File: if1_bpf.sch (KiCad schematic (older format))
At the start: 8 parts

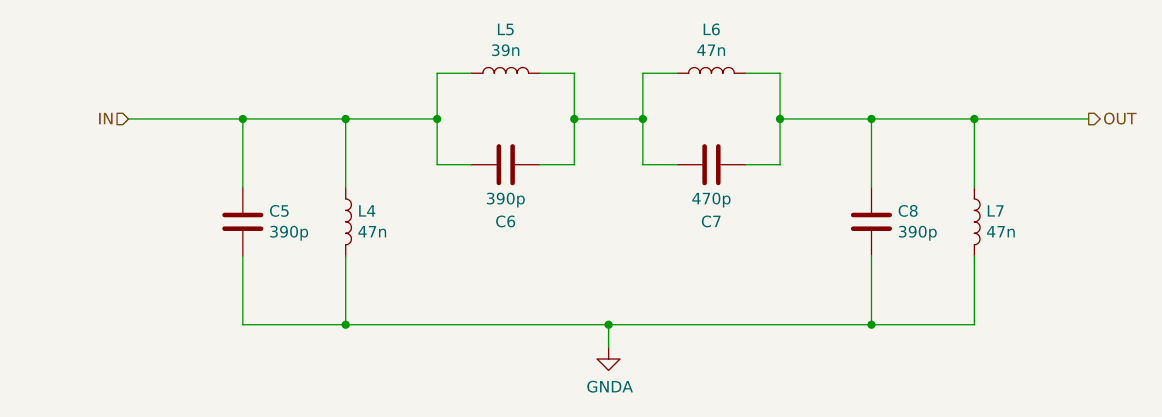
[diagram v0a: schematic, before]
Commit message: FPGA change and new project file
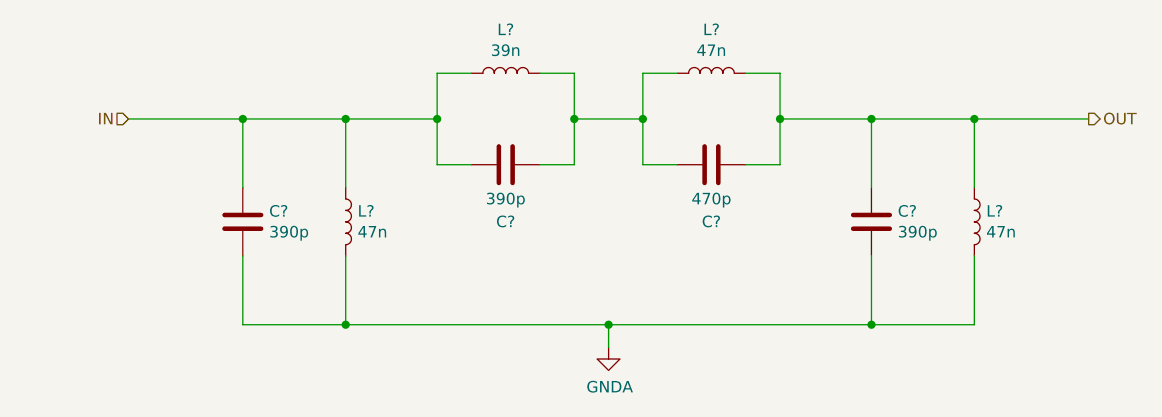
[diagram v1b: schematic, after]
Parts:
- renumbered C5 to C?, C6 to C?, C7 to C?, C8 to C?, L4 to L?, L5 to L?, L6 to L?, L7 to L?
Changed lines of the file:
@@
 $Descr A4 11693 8268
 encoding utf-8
-Sheet 3 7
+Sheet 3 12
 Title "37,224 MHz Bandpass filter"
 Date "2021 january"
@@
 OUT
 $Comp
-L Device:C C5
+L Device:C C?
 U 1 1 600431FC
 P 4450 3850
-F 0 "C5" H 4565 3896 50  0000 L CNN
+F 0 "C?" H 4565 3896 50  0000 L CNN
 F 1 "390p" H 4565 3805 50  0000 L CNN
 F 2 "Capacitor_SMD:C_0805_2012Metric_Pad1.18x1.45mm_HandSolder" H 4488 3700 50  0001 C CNN
@@
 $EndComp
 $Comp
-L Device:L L4
+L Device:L L?
 U 1 1 600436A2
 P 4900 3850
-F 0 "L4" H 4952 3896 50  0000 L CNN
+F 0 "L?" H 4952 3896 50  0000 L CNN
 F 1 "47n" H 4952 3805 50  0000 L CNN
 F 2 "Inductor_SMD:L_0603_1608Metric_Pad1.05x0.95mm_HandSolder" H 4900 3850 50  0001 C CNN
@@
 $EndComp
 $Comp
-L Device:L L5
+L Device:L L?
 U 1 1 600471E0
 P 5600 3200
-F 0 "L5" V 5790 3200 50  0000 C CNN
+F 0 "L?" V 5790 3200 50  0000 C CNN
 F 1 "39n" V 5699 3200 50  0000 C CNN
 F 2 "Inductor_SMD:L_0402_1005Metric_Pad0.77x0.64mm_HandSolder" H 5600 3200 50  0001 C CNN
@@
 $EndComp
 $Comp
-L Device:C C6
+L Device:C C?
 U 1 1 6004779D
 P 5600 3600
-F 0 "C6" V 5350 3600 50  0000 C CNN
+F 0 "C?" V 5350 3600 50  0000 C CNN
 F 1 "390p" V 5450 3600 50  0000 C CNN
 F 2 "Capacitor_SMD:C_0805_2012Metric_Pad1.18x1.45mm_HandSolder" H 5638 3450 50  0001 C CNN
@@
 $EndComp
 $Comp
-L Device:L L6
+L Device:L L?
 U 1 1 6004D573
 P 6500 3200
-F 0 "L6" V 6690 3200 50  0000 C CNN
+F 0 "L?" V 6690 3200 50  0000 C CNN
 F 1 "47n" V 6599 3200 50  0000 C CNN
 F 2 "Inductor_SMD:L_0603_1608Metric_Pad1.05x0.95mm_HandSolder" H 6500 3200 50  0001 C CNN
@@
 $EndComp
 $Comp
-L Device:C C7
+L Device:C C?
 U 1 1 6004D579
 P 6500 3600
-F 0 "C7" V 6250 3600 50  0000 C CNN
+F 0 "C?" V 6250 3600 50  0000 C CNN
 F 1 "470p" V 6350 3600 50  0000 C CNN
 F 2 "Capacitor_SMD:C_0805_2012Metric_Pad1.18x1.45mm_HandSolder" H 6538 3450 50  0001 C CNN
@@
 $EndComp
 $Comp
-L Device:C C8
+L Device:C C?
 U 1 1 6004E74D
 P 7200 3850
-F 0 "C8" H 7315 3896 50  0000 L CNN
+F 0 "C?" H 7315 3896 50  0000 L CNN
 F 1 "390p" H 7315 3805 50  0000 L CNN
 F 2 "Capacitor_SMD:C_0805_2012Metric_Pad1.18x1.45mm_HandSolder" H 7238 3700 50  0001 C CNN
@@
 $EndComp
 $Comp
-L Device:L L7
+L Device:L L?
 U 1 1 6004E753
 P 7650 3850
-F 0 "L7" H 7702 3896 50  0000 L CNN
+F 0 "L?" H 7702 3896 50  0000 L CNN
 F 1 "47n" H 7702 3805 50  0000 L CNN
 F 2 "Inductor_SMD:L_0603_1608Metric_Pad1.05x0.95mm_HandSolder" H 7650 3850 50  0001 C CNN
@@
 	6050 4300 7200 4300
 $Comp
-L power:GNDA #PWR0108
+L power:GNDA #PWR?
 U 1 1 60071173
 P 6050 4400
-F 0 "#PWR0108" H 6050 4150 50  0001 C CNN
+F 0 "#PWR?" H 6050 4150 50  0001 C CNN
 F 1 "GNDA" H 6055 4227 50  0000 C CNN
 F 2 "" H 6050 4400 50  0001 C CNN

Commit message: PCB is Done... Needs DRC check
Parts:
- gave numbers to parts that had none: 8
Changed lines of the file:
@@
 $Descr A4 11693 8268
 encoding utf-8
-Sheet 4 14
+Sheet 4 7
 Title "37,224 MHz Bandpass filter"
 Date "2021 january"
@@
 OUT
 $Comp
-L Device:C C?
+L Device:C C5
 U 1 1 600431FC
 P 4450 3850
-F 0 "C?" H 4565 3896 50  0000 L CNN
+F 0 "C5" H 4565 3896 50  0000 L CNN
 F 1 "390p" H 4565 3805 50  0000 L CNN
 F 2 "Capacitor_SMD:C_0805_2012Metric_Pad1.18x1.45mm_HandSolder" H 4488 3700 50  0001 C CNN
@@
 $EndComp
 $Comp
-L Device:L L?
+L Device:L L4
 U 1 1 600436A2
 P 4900 3850
-F 0 "L?" H 4952 3896 50  0000 L CNN
+F 0 "L4" H 4952 3896 50  0000 L CNN
 F 1 "47n" H 4952 3805 50  0000 L CNN
 F 2 "Inductor_SMD:L_0603_1608Metric_Pad1.05x0.95mm_HandSolder" H 4900 3850 50  0001 C CNN
@@
 $EndComp
 $Comp
-L Device:L L?
+L Device:L L5
 U 1 1 600471E0
 P 5600 3200
-F 0 "L?" V 5790 3200 50  0000 C CNN
+F 0 "L5" V 5790 3200 50  0000 C CNN
 F 1 "39n" V 5699 3200 50  0000 C CNN
 F 2 "Inductor_SMD:L_0402_1005Metric_Pad0.77x0.64mm_HandSolder" H 5600 3200 50  0001 C CNN
@@
 $EndComp
 $Comp
-L Device:C C?
+L Device:C C6
 U 1 1 6004779D
 P 5600 3600
-F 0 "C?" V 5350 3600 50  0000 C CNN
+F 0 "C6" V 5350 3600 50  0000 C CNN
 F 1 "390p" V 5450 3600 50  0000 C CNN
 F 2 "Capacitor_SMD:C_0805_2012Metric_Pad1.18x1.45mm_HandSolder" H 5638 3450 50  0001 C CNN
@@
 $EndComp
 $Comp
-L Device:L L?
+L Device:L L6
 U 1 1 6004D573
 P 6500 3200
-F 0 "L?" V 6690 3200 50  0000 C CNN
+F 0 "L6" V 6690 3200 50  0000 C CNN
 F 1 "47n" V 6599 3200 50  0000 C CNN
 F 2 "Inductor_SMD:L_0603_1608Metric_Pad1.05x0.95mm_HandSolder" H 6500 3200 50  0001 C CNN
@@
 $EndComp
 $Comp
-L Device:C C?
+L Device:C C7
 U 1 1 6004D579
 P 6500 3600
-F 0 "C?" V 6250 3600 50  0000 C CNN
+F 0 "C7" V 6250 3600 50  0000 C CNN
 F 1 "470p" V 6350 3600 50  0000 C CNN
 F 2 "Capacitor_SMD:C_0805_2012Metric_Pad1.18x1.45mm_HandSolder" H 6538 3450 50  0001 C CNN
@@
 $EndComp
 $Comp
-L Device:C C?
+L Device:C C8
 U 1 1 6004E74D
 P 7200 3850
-F 0 "C?" H 7315 3896 50  0000 L CNN
+F 0 "C8" H 7315 3896 50  0000 L CNN
 F 1 "390p" H 7315 3805 50  0000 L CNN
 F 2 "Capacitor_SMD:C_0805_2012Metric_Pad1.18x1.45mm_HandSolder" H 7238 3700 50  0001 C CNN
@@
 $EndComp
 $Comp
-L Device:L L?
+L Device:L L7
 U 1 1 6004E753
 P 7650 3850
-F 0 "L?" H 7702 3896 50  0000 L CNN
+F 0 "L7" H 7702 3896 50  0000 L CNN
 F 1 "47n" H 7702 3805 50  0000 L CNN
 F 2 "Inductor_SMD:L_0603_1608Metric_Pad1.05x0.95mm_HandSolder" H 7650 3850 50  0001 C CNN
@@
 	6050 4300 7200 4300
 $Comp
-L power:GNDA #PWR?
+L power:GNDA #PWR06
 U 1 1 60071173
 P 6050 4400
-F 0 "#PWR?" H 6050 4150 50  0001 C CNN
+F 0 "#PWR06" H 6050 4150 50  0001 C CNN
 F 1 "GNDA" H 6055 4227 50  0000 C CNN
 F 2 "" H 6050 4400 50  0001 C CNN

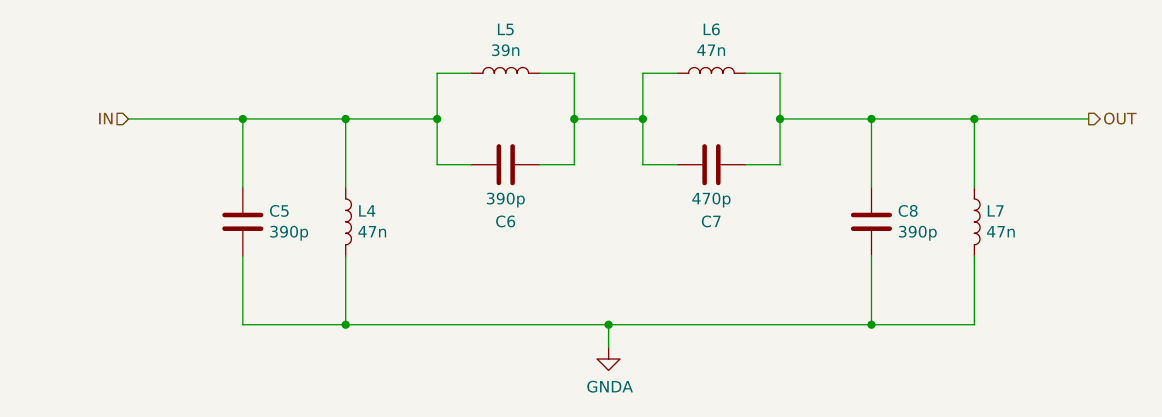
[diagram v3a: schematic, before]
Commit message: RX PCB revision: Diff amp + Mixer2
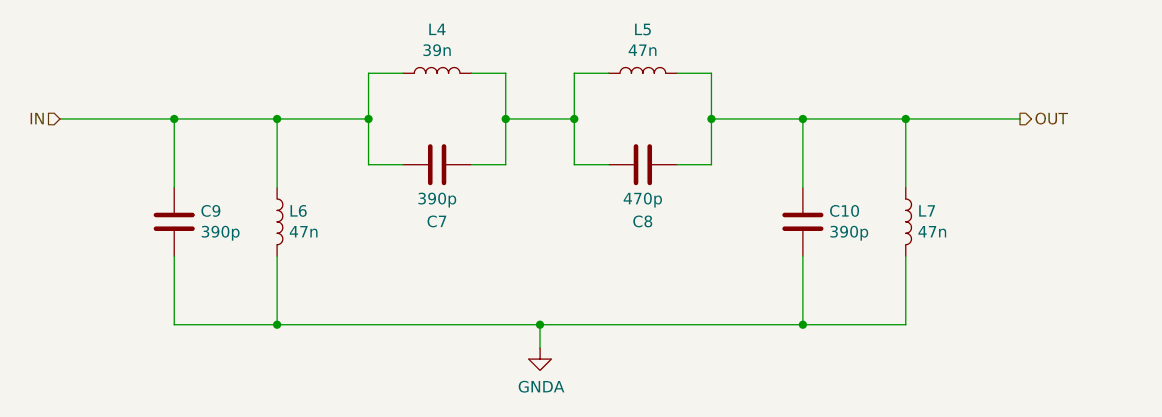
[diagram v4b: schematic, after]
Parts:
- C10: renamed from C8; footprint Capacitor_SMD:C_0805_2012Metric_Pad1.18x1.45mm_HandSolder -> Capacitor_SMD:C_0805_2012Metric_Pad1.15x1.40mm_HandSolder
- C7: renamed from C6; footprint Capacitor_SMD:C_0805_2012Metric_Pad1.18x1.45mm_HandSolder -> Capacitor_SMD:C_0805_2012Metric_Pad1.15x1.40mm_HandSolder
- C8: renamed from C7; footprint Capacitor_SMD:C_0805_2012Metric_Pad1.18x1.45mm_HandSolder -> Capacitor_SMD:C_0805_2012Metric_Pad1.15x1.40mm_HandSolder
- C9: renamed from C5; footprint Capacitor_SMD:C_0805_2012Metric_Pad1.18x1.45mm_HandSolder -> Capacitor_SMD:C_0805_2012Metric_Pad1.15x1.40mm_HandSolder
- renumbered L5 to L4, L6 to L5, L4 to L6
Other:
- moved on the sheet: C10, C7, C8, C9, L4, L5, L6, L7
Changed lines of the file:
@@
 $Descr A4 11693 8268
 encoding utf-8
-Sheet 4 7
+Sheet 3 7
 Title "37,224 MHz Bandpass filter"
 Date "2021 january"
-Rev "v02"
+Rev "v03"
 Comp "by Keri"
 Comment1 "50 Ohm input/output impedance"
@@
 Comment4 "Inverse Chebysev structure"
 $EndDescr
-Text HLabel 3950 3400 0    50   Input ~ 0
+Text HLabel 3650 3400 0    50   Input ~ 0
 IN
-Text HLabel 8150 3400 2    50   Output ~ 0
+Text HLabel 7850 3400 2    50   Output ~ 0
 OUT
 $Comp
-L Device:C C5
+L Device:C C9
 U 1 1 600431FC
-P 4450 3850
-F 0 "C5" H 4565 3896 50  0000 L CNN
-F 1 "390p" H 4565 3805 50  0000 L CNN
-F 2 "Capacitor_SMD:C_0805_2012Metric_Pad1.18x1.45mm_HandSolder" H 4488 3700 50  0001 C CNN
-F 3 "~" H 4450 3850 50  0001 C CNN
-	1    4450 3850
+P 4150 3850
+F 0 "C9" H 4265 3896 50  0000 L CNN
+F 1 "390p" H 4265 3805 50  0000 L CNN
+F 2 "Capacitor_SMD:C_0805_2012Metric_Pad1.15x1.40mm_HandSolder" H 4188 3700 50  0001 C CNN
+F 3 "~" H 4150 3850 50  0001 C CNN
+	1    4150 3850
+	1    0    0    -1
+$EndComp
+$Comp
+L Device:L L6
+U 1 1 600436A2
+P 4600 3850
+F 0 "L6" H 4652 3896 50  0000 L CNN
+F 1 "47n" H 4652 3805 50  0000 L CNN
+F 2 "Inductor_SMD:L_0603_1608Metric_Pad1.05x0.95mm_HandSolder" H 4600 3850 50  0001 C CNN
+F 3 "~" H 4600 3850 50  0001 C CNN
+F 4 "93-02-59" H 4600 3850 50  0001 C CNN "Lomex"
+	1    4600 3850
 	1    0    0    -1
 $EndComp
 $Comp
 L Device:L L4
-U 1 1 600436A2
-P 4900 3850
-F 0 "L4" H 4952 3896 50  0000 L CNN
-F 1 "47n" H 4952 3805 50  0000 L CNN
-F 2 "Inductor_SMD:L_0603_1608Metric_Pad1.05x0.95mm_HandSolder" H 4900 3850 50  0001 C CNN
-F 3 "~" H 4900 3850 50  0001 C CNN
-F 4 "93-02-59" H 4900 3850 50  0001 C CNN "Lomex"
-	1    4900 3850
-	1    0    0    -1
+U 1 1 600471E0
+P 5300 3200
+F 0 "L4" V 5490 3200 50  0000 C CNN
+F 1 "39n" V 5399 3200 50  0000 C CNN
+F 2 "Inductor_SMD:L_0402_1005Metric_Pad0.77x0.64mm_HandSolder" H 5300 3200 50  0001 C CNN
+F 3 "~" H 5300 3200 50  0001 C CNN
+F 4 "2846682RL" H 5300 3200 50  0001 C CNN "Farnell"
+	1    5300 3200
+	0    -1   -1   0
+$EndComp
+$Comp
+L Device:C C7
+U 1 1 6004779D
+P 5300 3600
+F 0 "C7" V 5050 3600 50  0000 C CNN
+F 1 "390p" V 5150 3600 50  0000 C CNN
+F 2 "Capacitor_SMD:C_0805_2012Metric_Pad1.15x1.40mm_HandSolder" H 5338 3450 50  0001 C CNN
+F 3 "~" H 5300 3600 50  0001 C CNN
+	1    5300 3600
+	0    -1   -1   0
 $EndComp
 $Comp
 L Device:L L5
-U 1 1 600471E0
-P 5600 3200
-F 0 "L5" V 5790 3200 50  0000 C CNN
-F 1 "39n" V 5699 3200 50  0000 C CNN
-F 2 "Inductor_SMD:L_0402_1005Metric_Pad0.77x0.64mm_HandSolder" H 5600 3200 50  0001 C CNN
-F 3 "~" H 5600 3200 50  0001 C CNN
-F 4 "2846682RL" H 5600 3200 50  0001 C CNN "Farnell"
-	1    5600 3200
-	0    -1   -1   0
-$EndComp
-$Comp
-L Device:C C6
-U 1 1 6004779D
-P 5600 3600
-F 0 "C6" V 5350 3600 50  0000 C CNN
-F 1 "390p" V 5450 3600 50  0000 C CNN
-F 2 "Capacitor_SMD:C_0805_2012Metric_Pad1.18x1.45mm_HandSolder" H 5638 3450 50  0001 C CNN
-F 3 "~" H 5600 3600 50  0001 C CNN
-	1    5600 3600
-	0    -1   -1   0
-$EndComp
-$Comp
-L Device:L L6
 U 1 1 6004D573
-P 6500 3200
-F 0 "L6" V 6690 3200 50  0000 C CNN
-F 1 "47n" V 6599 3200 50  0000 C CNN
-F 2 "Inductor_SMD:L_0603_1608Metric_Pad1.05x0.95mm_HandSolder" H 6500 3200 50  0001 C CNN
-F 3 "~" H 6500 3200 50  0001 C CNN
-F 4 "93-02-59" H 6500 3200 50  0001 C CNN "Lomex"
-	1    6500 3200
-	0    -1   -1   0
-$EndComp
-$Comp
-L Device:C C7
+P 6200 3200
+F 0 "L5" V 6390 3200 50  0000 C CNN
+F 1 "47n" V 6299 3200 50  0000 C CNN
+F 2 "Inductor_SMD:L_0603_1608Metric_Pad1.05x0.95mm_HandSolder" H 6200 3200 50  0001 C CNN
+F 3 "~" H 6200 3200 50  0001 C CNN
+F 4 "93-02-59" H 6200 3200 50  0001 C CNN "Lomex"
+	1    6200 3200
+	0    -1   -1   0
+$EndComp
+$Comp
+L Device:C C8
 U 1 1 6004D579
-P 6500 3600
-F 0 "C7" V 6250 3600 50  0000 C CNN
-F 1 "470p" V 6350 3600 50  0000 C CNN
-F 2 "Capacitor_SMD:C_0805_2012Metric_Pad1.18x1.45mm_HandSolder" H 6538 3450 50  0001 C CNN
-F 3 "~" H 6500 3600 50  0001 C CNN
-	1    6500 3600
-	0    -1   -1   0
-$EndComp
-$Comp
-L Device:C C8
+P 6200 3600
+F 0 "C8" V 5950 3600 50  0000 C CNN
+F 1 "470p" V 6050 3600 50  0000 C CNN
+F 2 "Capacitor_SMD:C_0805_2012Metric_Pad1.15x1.40mm_HandSolder" H 6238 3450 50  0001 C CNN
+F 3 "~" H 6200 3600 50  0001 C CNN
+	1    6200 3600
+	0    -1   -1   0
+$EndComp
+$Comp
+L Device:C C10
 U 1 1 6004E74D
-P 7200 3850
-F 0 "C8" H 7315 3896 50  0000 L CNN
-F 1 "390p" H 7315 3805 50  0000 L CNN
-F 2 "Capacitor_SMD:C_0805_2012Metric_Pad1.18x1.45mm_HandSolder" H 7238 3700 50  0001 C CNN
-F 3 "~" H 7200 3850 50  0001 C CNN
-	1    7200 3850
+P 6900 3850
+F 0 "C10" H 7015 3896 50  0000 L CNN
+F 1 "390p" H 7015 3805 50  0000 L CNN
+F 2 "Capacitor_SMD:C_0805_2012Metric_Pad1.15x1.40mm_HandSolder" H 6938 3700 50  0001 C CNN
+F 3 "~" H 6900 3850 50  0001 C CNN
+	1    6900 3850
 	1    0    0    -1
 $EndComp
@@
 L Device:L L7
 U 1 1 6004E753
-P 7650 3850
-F 0 "L7" H 7702 3896 50  0000 L CNN
-F 1 "47n" H 7702 3805 50  0000 L CNN
-F 2 "Inductor_SMD:L_0603_1608Metric_Pad1.05x0.95mm_HandSolder" H 7650 3850 50  0001 C CNN
-F 3 "~" H 7650 3850 50  0001 C CNN
-F 4 "93-02-59" H 7650 3850 50  0001 C CNN "Lomex"
-	1    7650 3850
-	1    0    0    -1
-$EndComp
-Wire Wire Line
-	5750 3600 5900 3600
-Wire Wire Line
-	5900 3600 5900 3400
-Wire Wire Line
-	5900 3200 5750 3200
-Wire Wire Line
-	5450 3600 5300 3600
-Wire Wire Line
-	5300 3600 5300 3400
-Wire Wire Line
-	5300 3200 5450 3200
-Wire Wire Line
-	6350 3200 6200 3200
-Wire Wire Line
-	6200 3200 6200 3400
-Wire Wire Line
-	6200 3600 6350 3600
-Wire Wire Line
-	6650 3600 6800 3600
-Wire Wire Line
-	6800 3600 6800 3400
-Wire Wire Line
-	6800 3200 6650 3200
-Wire Wire Line
-	5900 3400 6200 3400
+P 7350 3850
+F 0 "L7" H 7402 3896 50  0000 L CNN
+F 1 "47n" H 7402 3805 50  0000 L CNN
+F 2 "Inductor_SMD:L_0603_1608Metric_Pad1.05x0.95mm_HandSolder" H 7350 3850 50  0001 C CNN
+F 3 "~" H 7350 3850 50  0001 C CNN
+F 4 "93-02-59" H 7350 3850 50  0001 C CNN "Lomex"
+	1    7350 3850
+	1    0    0    -1
+$EndComp
+Wire Wire Line
+	5450 3600 5600 3600
+Wire Wire Line
+	5600 3600 5600 3400
+Wire Wire Line
+	5600 3200 5450 3200
+Wire Wire Line
+	5150 3600 5000 3600
+Wire Wire Line
+	5000 3600 5000 3400
+Wire Wire Line
+	5000 3200 5150 3200
+Wire Wire Line
+	6050 3200 5900 3200
+Wire Wire Line
+	5900 3200 5900 3400
+Wire Wire Line
+	5900 3600 6050 3600
+Wire Wire Line
+	6350 3600 6500 3600
+Wire Wire Line
+	6500 3600 6500 3400
+Wire Wire Line
+	6500 3200 6350 3200
+Wire Wire Line
+	5600 3400 5900 3400
+Connection ~ 5600 3400
+Wire Wire Line
+	5600 3400 5600 3200
 Connection ~ 5900 3400
 Wire Wire Line
-	5900 3400 5900 3200
-Connection ~ 6200 3400
-Wire Wire Line
-	6200 3400 6200 3600
-Connection ~ 5300 3400
-Wire Wire Line
-	5300 3400 5300 3200
-Connection ~ 6800 3400
-Wire Wire Line
-	6800 3400 6800 3200
-Wire Wire Line
-	4450 3400 4900 3400
-Wire Wire Line
-	6800 3400 7200 3400
-Wire Wire Line
-	4450 3700 4450 3400
-Wire Wire Line
-	4900 3700 4900 3400
-Connection ~ 4900 3400
-Wire Wire Line
-	4900 3400 5300 3400
-Wire Wire Line
-	7200 3700 7200 3400
-Connection ~ 7200 3400
-Wire Wire Line
-	7200 3400 7650 3400
-Wire Wire Line
-	7650 3700 7650 3400
-Wire Wire Line
-	4450 4000 4450 4300
-Wire Wire Line
-	4450 4300 4900 4300
-Wire Wire Line
-	7650 4300 7650 4000
-Wire Wire Line
-	7200 4000 7200 4300
-Connection ~ 7200 4300
-Wire Wire Line
-	7200 4300 7650 4300
-Wire Wire Line
-	4900 4000 4900 4300
-Connection ~ 4900 4300
-Wire Wire Line
-	4900 4300 6050 4300
-Wire Wire Line
-	6050 4300 6050 4400
-Connection ~ 6050 4300
-Wire Wire Line
-	6050 4300 7200 4300
-$Comp
-L power:GNDA #PWR06
-U 1 1 60071173
-P 6050 4400
-F 0 "#PWR06" H 6050 4150 50  0001 C CNN
-F 1 "GNDA" H 6055 4227 50  0000 C CNN
-F 2 "" H 6050 4400 50  0001 C CNN
-F 3 "" H 6050 4400 50  0001 C CNN
-	1    6050 4400
-	1    0    0    -1
-$EndComp
-Wire Wire Line
-	8150 3400 7650 3400
-Connection ~ 7650 3400
-Wire Wire Line
-	4450 3400 3950 3400
-Connection ~ 4450 3400
+	5900 3400 5900 3600
+Connection ~ 5000 3400
+Wire Wire Line
+	5000 3400 5000 3200
+Connection ~ 6500 3400
+Wire Wire Line
+	6500 3400 6500 3200
+Wire Wire Line
+	4150 3400 4600 3400
+Wire Wire Line
+	6500 3400 6900 3400
+Wire Wire Line
+	4150 3700 4150 3400
+Wire Wire Line
+	4600 3700 4600 3400
+Connection ~ 4600 3400
+Wire Wire Line
+	4600 3400 5000 3400
+Wire Wire Line
+	6900 3700 6900 3400
+Connection ~ 6900 3400
+Wire Wire Line
+	6900 3400 7350 3400
+Wire Wire Line
+	7350 3700 7350 3400
+Wire Wire Line
+	4150 4000 4150 4300
+Wire Wire Line
+	4150 4300 4600 4300
+Wire Wire Line
+	7350 4300 7350 4000
+Wire Wire Line
+	6900 4000 6900 4300
+Connection ~ 6900 4300
+Wire Wire Line
+	6900 4300 7350 4300
+Wire Wire Line
+	4600 4000 4600 4300
+Connection ~ 4600 4300
+Wire Wire Line
+	4600 4300 5750 4300
+Wire Wire Line
+	5750 4300 5750 4400
+Connection ~ 5750 4300
+Wire Wire Line
+	5750 4300 6900 4300
+Wire Wire Line
+	4150 3400 3650 3400
+Connection ~ 4150 3400
+Wire Wire Line
+	7850 3400 7350 3400
+Connection ~ 7350 3400
+$Comp
+L power:GNDA #PWR015
+U 1 1 600AC268
+P 5750 4400
+F 0 "#PWR015" H 5750 4150 50  0001 C CNN
+F 1 "GNDA" H 5755 4227 50  0000 C CNN
+F 2 "" H 5750 4400 50  0001 C CNN
+F 3 "" H 5750 4400 50  0001 C CNN
+	1    5750 4400
+	1    0    0    -1
+$EndComp
 $EndSCHEMATC
